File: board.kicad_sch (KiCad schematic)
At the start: 16 parts, among them J2 Conn_2Rows-33Pins, J3 Conn_2Rows-33Pins, J4 Conn_2Rows-33Pins, J5 Conn_2Rows-33Pins, J6 Conn_2Rows-33Pins, U1 MC68060RC50, U10 74LVC162245ADGG, U11 74LVC162245ADGG, U2 XC95144XL-5TQG100C, U3 SST39VF1601C-70-4C-EKE, U4 IS61WV51216BLL-10TLI, U5 IS61WV51216BLL-10TLI, U6 SST39VF1601C-70-4C-EKE, U7 74LVC162245ADGG, U8 74LVC162245ADGG, U9 74LVC162245ADGG

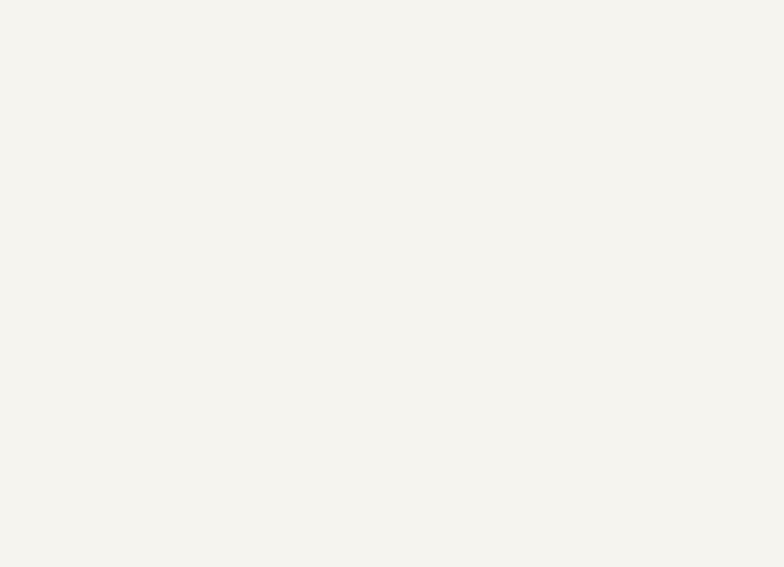
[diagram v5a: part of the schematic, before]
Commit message: Added clock chip
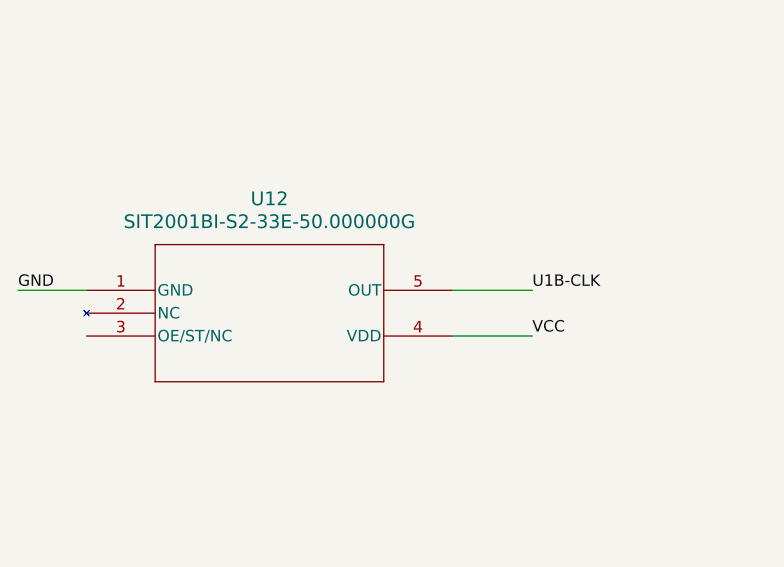
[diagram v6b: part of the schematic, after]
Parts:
- added U12: SIT2001BI-S2-33E-50.000000G, SOT_SiT1630-S_SIT, symbol Clock:SIT2001BI-S2-33E-50.000000G
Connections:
- net GND: now also U12.1 (GND)
- net U1B-CLK: now also U12.5 (OUT)
- net VCC: now also U12.4 (VDD)
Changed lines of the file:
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@@
 	(wire
 		(pts
+			(xy 74.93 264.16) (xy 82.55 264.16)
+		)
+		(stroke
+			(width 0)
+			(type default)
+		)
+	)
+	(wire
+		(pts
 			(xy 547.37 289.56) (xy 557.53 289.56)
 		)
@@
 	(wire
 		(pts
+			(xy 123.19 269.24) (xy 132.08 269.24)
+		)
+		(stroke
+			(width 0)
+			(type default)
+		)
+	)
+	(wire
+		(pts
 			(xy 440.69 297.18) (xy 445.77 297.18)
 		)
@@
 	(wire
 		(pts
+			(xy 123.19 264.16) (xy 132.08 264.16)
+		)
+		(stroke
+			(width 0)
+			(type default)
+		)
+	)
+	(wire
+		(pts
 			(xy 549.91 233.68) (xy 557.53 233.68)
 		)
@@
 		)
 	)
+	(label "GND"
+		(at 74.93 264.16 0)
+		(effects
+			(font
+				(size 1.27 1.27)
+			)
+			(justify left bottom)
+		)
+	)
 	(label "A13"
 		(at 236.22 128.27 0)
@@
 		)
 	)
+	(label "U1B-CLK"
+		(at 132.08 264.16 0)
+		(effects
+			(font
+				(size 1.27 1.27)
+			)
+			(justify left bottom)
+		)
+	)
 	(label "EXT_D30"
 		(at 557.53 243.84 0)
@@
 		)
 	)
+	(label "VCC"
+		(at 132.08 269.24 0)
+		(effects
+			(font
+				(size 1.27 1.27)
+			)
+			(justify left bottom)
+		)
+	)
 	(label "EXT_D[0..15]"
 		(at 537.21 105.41 0)
@@
 					(unit 1)
 				)
+			)
+		)
+	)
+	(symbol
+		(lib_id "Clock:SIT2001BI-S2-33E-50.000000G")
+		(at 82.55 264.16 0)
+		(unit 1)
+		(body_style 1)
+		(exclude_from_sim no)
+		(in_bom yes)
+		(on_board yes)
+		(in_pos_files yes)
+		(dnp no)
+		(fields_autoplaced yes)
+		(property "Reference" "U12"
+			(at 102.87 254 0)
+			(show_name no)
+			(do_not_autoplace no)
+			(effects
+				(font
+					(size 1.524 1.524)
+				)
+			)
+		)
+		(property "Value" "SIT2001BI-S2-33E-50.000000G"
+			(at 102.87 256.54 0)
+			(show_name no)
+			(do_not_autoplace no)
+			(effects
+				(font
+					(size 1.524 1.524)
+				)
+			)
+		)
+		(property "Footprint" "SOT_SiT1630-S_SIT"
+			(at 82.55 264.16 0)
+			(hide yes)
+			(show_name no)
+			(do_not_autoplace no)
+			(effects
+				(font
+					(size 1.27 1.27)
+					(italic yes)
+				)
+			)
+		)
+		(property "Datasheet" "SIT2001BI-S2-33E-50.000000G"
+			(at 82.55 264.16 0)
+			(hide yes)
+			(show_name no)
+			(do_not_autoplace no)
+			(effects
+				(font
+					(size 1.27 1.27)
+					(italic yes)
+				)
+			)
+		)
+		(property "Description" ""
+			(at 82.55 264.16 0)
+			(hide yes)
+			(show_name no)
+			(do_not_autoplace no)
+			(effects
+				(font
+					(size 1.27 1.27)
+				)
+			)
+		)
+		(pin "1"
+		)
+		(pin "3"
+		)
+		(pin "4"
+		)
+		(pin "5"
+		)
+		(pin "2"
+		)
+		(instances
+			(project "board"
+				(path "/27e6fb8b-ebcf-4ece-872b-7722c171602a"
+					(reference "U12")
+					(unit 1)
+				)

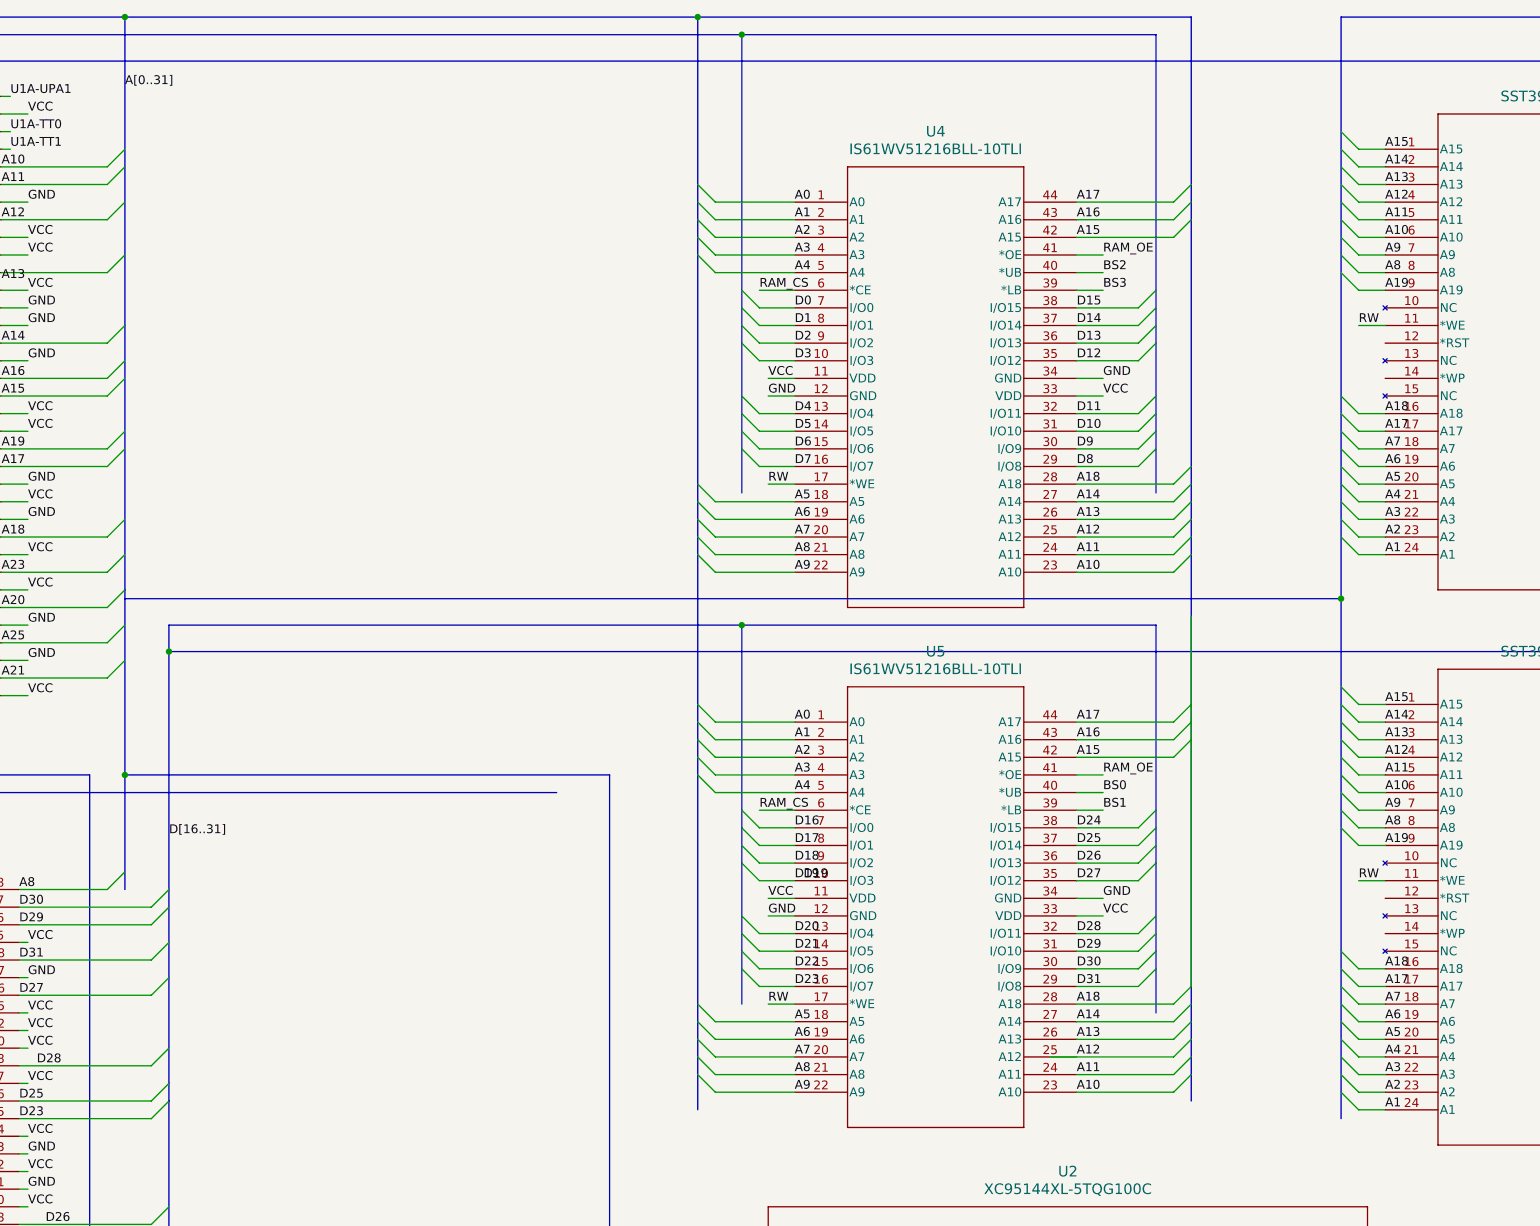
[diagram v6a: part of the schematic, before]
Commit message: Added A20 to eproms
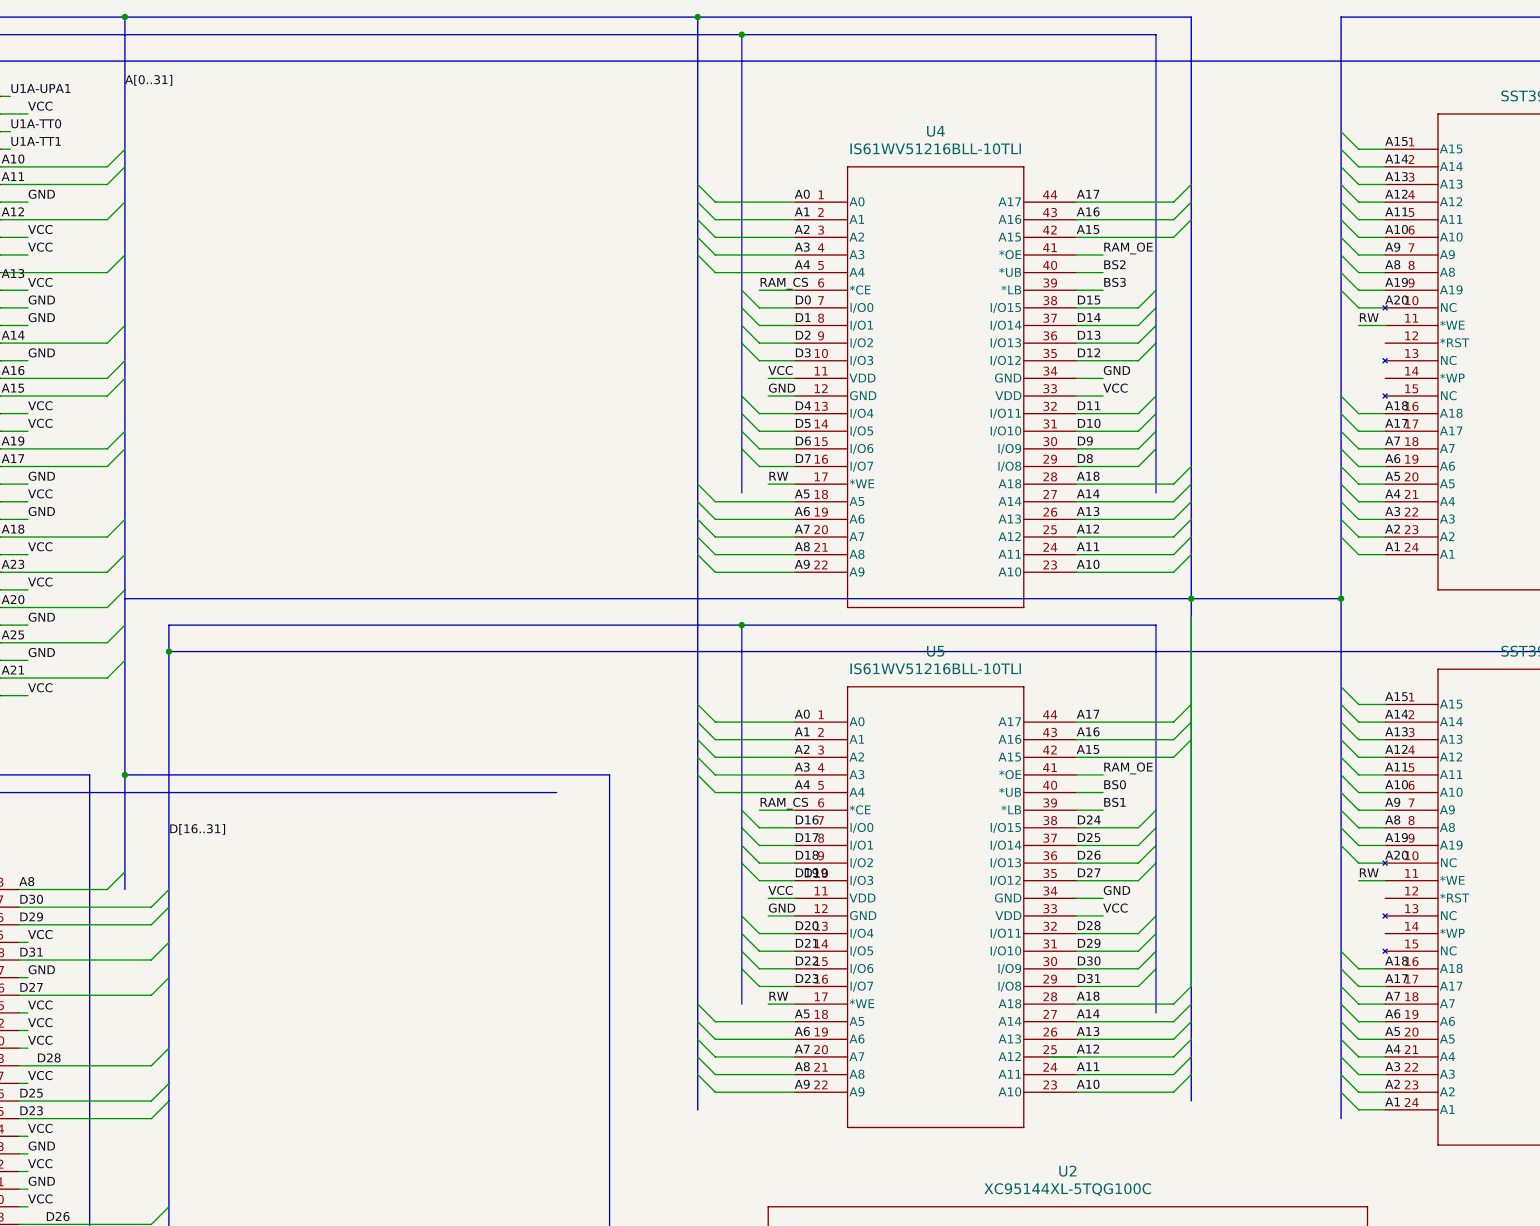
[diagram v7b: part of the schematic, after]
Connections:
- net A20: now also U3.10 (NC), U6.10 (NC)
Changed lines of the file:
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@@
 	)
 	(junction
+		(at 407.67 173.99)
+		(diameter 0)
+		(color 0 0 0 0)
+	)
+	(junction
 		(at 709.93 246.38)
 		(diameter 0)
@@
 	)
 	(bus_entry
+		(at 429.26 129.54)
+		(size 2.54 2.54)
+		(stroke
+			(width 0)
+			(type default)
+		)
+	)
+	(bus_entry
 		(at 734.06 429.26)
 		(size -2.54 2.54)
@@
 	)
 	(bus_entry
+		(at 429.26 209.55)
+		(size 2.54 2.54)
+		(stroke
+			(width 0)
+			(type default)
+		)
+	)
+	(bus_entry
 		(at 731.52 290.83)
 		(size -2.54 2.54)
@@
 		)
 	)
+	(bus
+		(pts
+			(xy 407.67 173.99) (xy 407.67 246.38)
+		)
+		(stroke
+			(width 0)
+			(type default)
+		)
+	)
 	(wire
 		(pts
@@
 	(wire
 		(pts
+			(xy 431.8 132.08) (xy 435.61 132.08)
+		)
+		(stroke
+			(width 0)
+			(type default)
+		)
+	)
+	(wire
+		(pts
 			(xy 709.93 339.09) (xy 709.93 341.63)
 		)
@@
 		)
 	)
-	(bus
-		(pts
-			(xy 254 172.72) (xy 254 199.39)
-		)
-		(stroke
-			(width 0)
-			(type default)
-		)
-	)
 	(wire
 		(pts
@@
 	(bus
 		(pts
+			(xy 407.67 173.99) (xy 429.26 173.99)
+		)
+		(stroke
+			(width 0)
+			(type default)
+		)
+	)
+	(bus
+		(pts
 			(xy 731.52 265.43) (xy 731.52 311.15)
 		)
@@
 	(bus
 		(pts
+			(xy 254 172.72) (xy 254 199.39)
+		)
+		(stroke
+			(width 0)
+			(type default)
+		)
+	)
+	(bus
+		(pts
 			(xy 260.35 181.61) (xy 260.35 243.84)
 		)
@@
 	(wire
 		(pts
+			(xy 431.8 212.09) (xy 435.61 212.09)
+		)
+		(stroke
+			(width 0)
+			(type default)
+		)
+	)
+	(wire
+		(pts
 			(xy 238.76 261.62) (xy 240.03 261.62)
 		)
@@
 	(bus
 		(pts
-			(xy 254 173.99) (xy 429.26 173.99)
+			(xy 254 173.99) (xy 407.67 173.99)
 		)
 		(stroke
@@
 	(bus
 		(pts
-			(xy 407.67 90.17) (xy 407.67 246.38)
+			(xy 407.67 90.17) (xy 407.67 173.99)
 		)
 		(stroke
@@
 		)
 	)
+	(label "A20"
+		(at 435.61 212.09 0)
+		(effects
+			(font
+				(size 1.27 1.27)
+			)
+			(justify left bottom)
+		)
+	)
 	(label "A9"
 		(at 618.49 314.96 0)
@@
 		(effects
 			(font
+				(size 1.27 1.27)
+			)
+			(justify left bottom)
+		)
+	)
+	(label "A20"
+		(at 435.61 132.08 0)
+		(effects
+			(font

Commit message: Added ext bus control lines
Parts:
- added J7: Conn_2Rows-33Pins, Connector_PinHeader_2.54mm:PinHeader_2x17_P2.54mm_Vertical, symbol Connector_Generic:Conn_2Rows-33Pins
- added U13: 74LVC162245ADGG, SOT362-1_NEX, symbol 7416254 buffer:74LVC16245ADGG
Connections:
- net U1B-TD0 is gone; now on net U1A-TT0: U2.83 (TDO)
- net BS0: now also U2.80 (NC); no longer U2.76 (NC)
- net BS1: now also U2.79 (NC); no longer U2.78 (NC)
- net BS2: now also U2.78 (NC); no longer U2.72 (NC)
- net BS3: now also U2.74 (NC); no longer U2.68 (NC)
- net GND: now also J6.1 (Pin_1), J6.11 (Pin_11), J6.13 (Pin_13), J6.15 (Pin_15), J6.17 (Pin_17), J6.19 (Pin_19), J6.21 (Pin_21), J6.23 (Pin_23), J6.25 (Pin_25), J6.27 (Pin_27), J6.29 (Pin_29), J6.3 (Pin_3), J6.31 (Pin_31), J6.33 (Pin_33), J6.5 (Pin_5), J6.7 (Pin_7), J6.9 (Pin_9), U10.10 (GND), U10.15 (GND), U10.21 (GND), U10.28 (GND), U10.34 (GND), U10.39 (GND), U10.4 (GND), U10.45 (GND), U11.10 (GND), U11.15 (GND), U11.21 (GND), U11.28 (GND), U11.34 (GND), U11.39 (GND), U11.4 (GND), U11.45 (GND), J7.1 (Pin_1), J7.11 (Pin_11), J7.13 (Pin_13), J7.15 (Pin_15), J7.17 (Pin_17), J7.19 (Pin_19), J7.21 (Pin_21), J7.23 (Pin_23), J7.25 (Pin_25), J7.27 (Pin_27), J7.29 (Pin_29), J7.3 (Pin_3), J7.31 (Pin_31), J7.33 (Pin_33), J7.5 (Pin_5), J7.7 (Pin_7), J7.9 (Pin_9), U13.10 (GND), U13.15 (GND), U13.21 (GND), U13.28 (GND), U13.34 (GND), U13.39 (GND), U13.4 (GND), U13.45 (GND)
- net U1A-TT0: no longer U2.82 (NC)
- net U1B-CLK: now also U11.47 (1A0), U2.22 (I/O/GCK1), U2.68 (NC); no longer U2.63 (NC)
- net U1B-CLKEN: now also U11.46 (1A1), U2.71 (NC); no longer U2.65 (NC)
- net U1B-IPL0: now also U2.70 (NC); no longer U2.64 (NC)
- net U1B-IPL1: now also U2.72 (NC); no longer U2.66 (NC)
- net U1B-IPL2: now also U2.76 (NC); no longer U2.70 (NC)
- net U1B-MDIS: now also U2.77 (NC); no longer U2.71 (NC)
- net U1B-RSTI: now also U2.73 (NC); no longer U2.67 (NC)
- net U1B-RSTO: now also U2.81 (NC); no longer U2.80 (NC)
- net U1B-TCK: no longer U2.74 (NC)
- net U1B-TDI: no longer U2.79 (NC)
- net U1B-TMS: no longer U2.73 (NC)
- net U1B-UPA0: now also U2.82 (NC); no longer U2.81 (NC)
- net U1C-AVEC: now also U2.66 (NC); no longer U2.60 (NC)
- net U1C-CLA: now also U2.49 (IO); no longer U2.47 (IO)
- net U1C-PST0: now also U2.54 (IO); no longer U2.52 (IO)
- net U1C-PST1: now also U2.56 (IO); no longer U2.54 (IO)
- net U1C-PST2: now also U2.61 (NC); no longer U2.56 (IO)
- net U1C-PST3: now also U2.52 (IO); no longer U2.49 (IO)
- net U1C-PST4: now also U2.64 (NC); no longer U2.59 (NC)
- net U1C-RW: now also U2.53 (IO); no longer U2.50 (IO)
- net U1C-SAS: now also U2.63 (NC); no longer U2.58 (NC)
- net U1C-TA: now also U2.58 (NC); no longer U2.55 (IO)
- net U1C-TCI: now also U2.67 (NC); no longer U2.61 (NC)
- net U1C-TIP: now also U2.55 (IO); no longer U2.53 (IO)
- net U1C-TM2: now also U2.47 (IO); no longer U2.46 (IO)
- net U1C-TS: now also U2.50 (IO); no longer U2.48 (IO)
- net VCC: now also U10.18 (VCC), U10.31 (VCC), U10.42 (VCC), U10.7 (VCC), U11.18 (VCC), U11.31 (VCC), U11.42 (VCC), U11.7 (VCC), U13.18 (VCC), U13.31 (VCC), U13.42 (VCC), U13.7 (VCC)
- net CPLD_X0: now reaches U2.11 (IO)
- net CPLD_X0: now also U11.36 (2A0)
- net CPLD_X1: now reaches U2.12 (IO)
- net CPLD_X1: now also U11.35 (2A1)
- net CPLD_X2: now reaches U2.13 (IO)
- net CPLD_X2: now also U11.33 (2A2)
- net CPLD_X3: now reaches U2.14 (IO)
- net CPLD_X3: now also U11.32 (2A3)
- net CPLD_X4: now reaches U2.15 (IO)
- net CPLD_X4: now also U11.30 (2A4)
- net CPLD_X5: now reaches U2.16 (IO)
- net CPLD_X5: now also U11.29 (2A5)
- net CPLD_X6: now reaches U2.17 (IO)
- net CPLD_X6: now also U11.27 (2A6)
- net CPLD_X7: now reaches U2.18 (IO)
- net CPLD_X7: now also U11.26 (2A7)
- net CPLD_XIN0: now reaches U2.19 (IO)
- net CPLD_XIN0: now also U13.47 (1A0)
- net CPLD_XIN1: now reaches U2.20 (IO)
- net CPLD_XIN1: now also U13.46 (1A1)
- net CPLD_XIN2: now reaches U2.23 (I/O/GCK2)
- net CPLD_XIN2: now also U13.44 (1A2)
- net CPLD_XIN3: now reaches U2.24 (IO)
- net CPLD_XIN3: now also U13.43 (1A3)
- net CPLD_XIN4: now reaches U2.25 (IO)
- net CPLD_XIN4: now also U13.41 (1A4)
- net CPLD_XIN5: now reaches U2.27 (I/O/GCK3)
- net CPLD_XIN5: now also U13.40 (1A5)
- net CPLD_XIN6: now reaches U2.28 (IO)
- net CPLD_XIN6: now also U13.38 (1A6)
- net CPLD_XIN7: now reaches U2.29 (IO)
- net CPLD_XIN7: now also U13.37 (1A7)
- net U1C-BGR: now reaches U1.Q11 (*BGR)
- net U1C-BGR: now also U2.65 (NC)
- net U1C-BTT: now reaches U1.Q15 (*BTT)
- net U1C-BTT: now also U2.59 (NC)
- net U1C-BG: now reaches U1.T13 (*BG)
- net U1C-BG: now also U2.60 (NC)
- net U1C-BB: now reaches U1.T17 (*BB)
- net U1C-BB: now also U2.48 (IO)
- net U1C-BR: now reaches U1.T18 (*BR)
- net U1C-BR: now also U2.46 (IO)
- net EXT_CTRLOUT4: now reaches J6.10 (Pin_10)
- net EXT_CTRLOUT4: now also U11.8 (1B4)
- net EXT_CTRLOUT5: now reaches J6.12 (Pin_12)
- net EXT_CTRLOUT5: now also U11.9 (1B5)
- net EXT_CTRLOUT6: now reaches J6.14 (Pin_14)
- net EXT_CTRLOUT6: now also U11.11 (1B6)
- net EXT_CTRLOUT7: now reaches J6.16 (Pin_16)
- net EXT_CTRLOUT7: now also U11.12 (1B7)
- net EXT_CTRLOUT8: now reaches J6.18 (Pin_18)
- net EXT_CTRLOUT8: now also U11.13 (2B0)
- net EXT_CTRLOUT0: now reaches J6.2 (Pin_2)
- net EXT_CTRLOUT0: now also U11.2 (1B0)
- net EXT_CTRLOUT9: now reaches J6.20 (Pin_20)
- net EXT_CTRLOUT9: now also U11.14 (2B1)
- net EXT_CTRLOUT10: now reaches J6.22 (Pin_22)
- net EXT_CTRLOUT10: now also U11.16 (2B2)
- net EXT_CTRLOUT11: now reaches J6.24 (Pin_24)
- net EXT_CTRLOUT11: now also U11.17 (2B3)
- net EXT_CTRLOUT12: now reaches J6.26 (Pin_26)
- net EXT_CTRLOUT12: now also U11.19 (2B4)
- net EXT_CTRLOUT13: now reaches J6.28 (Pin_28)
- net EXT_CTRLOUT13: now also U11.20 (2B5)
- net EXT_CTRLOUT14: now reaches J6.30 (Pin_30)
- net EXT_CTRLOUT14: now also U11.22 (2B6)
- net EXT_CTRLOUT15: now reaches J6.32 (Pin_32)
- net EXT_CTRLOUT15: now also U11.23 (2B7)
- net EXT_CTRLOUT1: now reaches J6.4 (Pin_4)
- net EXT_CTRLOUT1: now also U11.3 (1B1)
- net EXT_CTRLOUT2: now reaches J6.6 (Pin_6)
- net EXT_CTRLOUT2: now also U11.5 (1B2)
- net EXT_CTRLOUT3: now reaches J6.8 (Pin_8)
- net EXT_CTRLOUT3: now also U11.6 (1B3)
- new net EXT_CTRLIN0: J7.2 (Pin_2), U13.2 (1B0)
- new net EXT_CTRLIN1: J7.4 (Pin_4), U13.3 (1B1)
- new net EXT_CTRLIN2: J7.6 (Pin_6), U13.5 (1B2)
- new net EXT_CTRLIN3: J7.8 (Pin_8), U13.6 (1B3)
- new net EXT_CTRLIN4: J7.10 (Pin_10), U13.8 (1B4)
- new net EXT_CTRLIN5: J7.12 (Pin_12), U13.9 (1B5)
- new net EXT_CTRLIN6: J7.14 (Pin_14), U13.11 (1B6)
- new net EXT_CTRLIN7: J7.16 (Pin_16), U13.12 (1B7)
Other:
- moved on the sheet: J2, J3, J4, J5, J6, U10, U11, U12, U1A, U1B, U1C, U2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
